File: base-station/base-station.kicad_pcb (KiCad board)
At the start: 4 copper layers, 86.5 x 54 mm, 48 parts, among them J1 Conn_01x06, J2 USB_C_Receptacle_USB2.0_16P, J3 Conn_01x08, J4 Conn_01x02, J5 Conn_01x02, SW1 SW_Push, SW2 SW_SPDT, SW3 SW_SPDT, SW4 SW_Push, SW5 SW_Push, SW6 SW_Push, U1 MCP73832-2-OT, U2 AP2112K-3.3, U3 W25Q128JVS, U4 STM32G431KBTx, Y1 16MHz

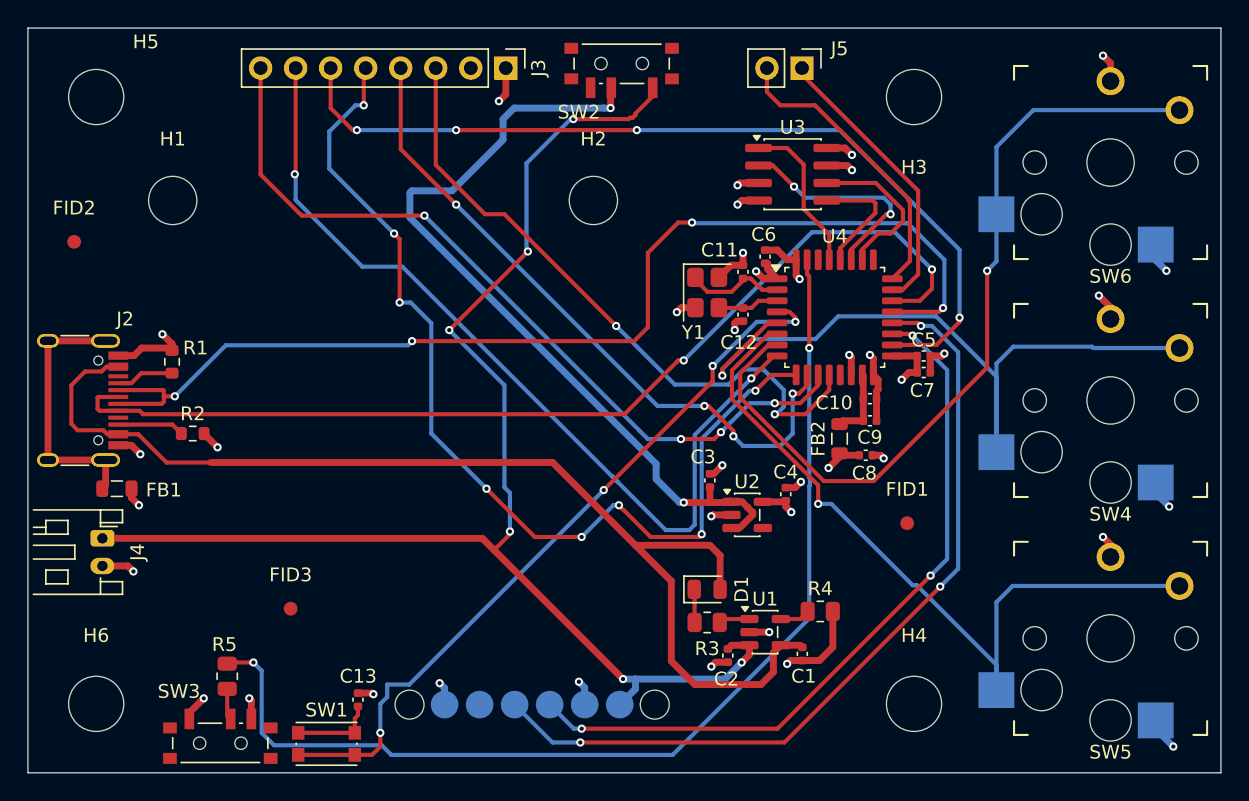
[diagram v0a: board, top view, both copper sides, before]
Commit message: add theming
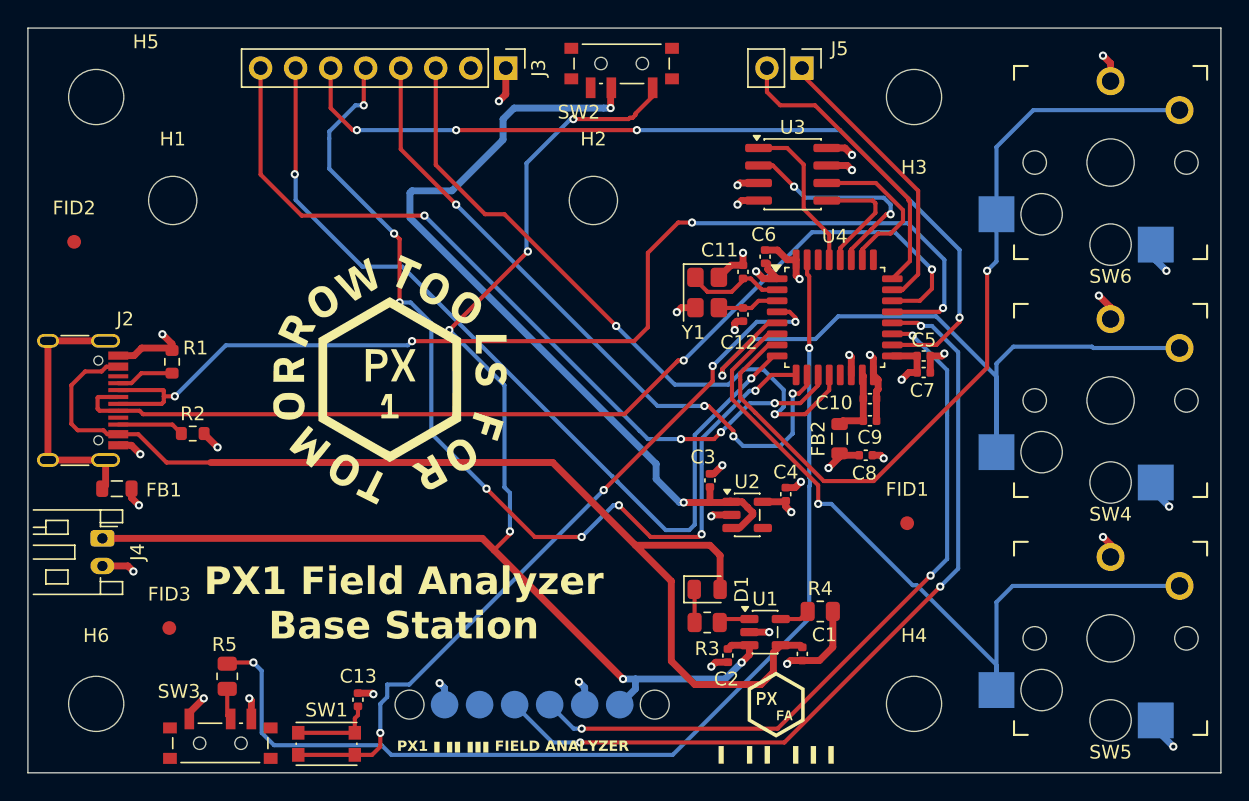
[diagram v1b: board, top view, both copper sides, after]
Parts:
- added G***: LOGO, LOGO, F.Cu at (60.5, 75.5)
- added G***: LOGO, LOGO, F.Cu at (88.5, 99.1)
- moved FID3 8.91 mm to (44.5, 93.5)
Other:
- board text added: "PX1 Field Analyzer Base Station"
- board text added: "PX1 ▮ ▮▮ ▮▮▮ FIELD ANALYZER"

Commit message: add mfg files
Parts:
- U3: footprint Package_SO:SOIC-8_3.9x4.9mm_P1.27mm -> Package_SO:SOIC-8_5.3x5.3mm_P1.27mm
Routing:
- net /FLASH_SCK: track 11.7 -> 10.6 mm
- net /FLASH_MOSI: track 8.76 -> 7.65 mm
- net /FLASH_MISO: track 16.1 -> 17.2 mm
- net /FLASH_CS: track 11.4 -> 12.6 mm
